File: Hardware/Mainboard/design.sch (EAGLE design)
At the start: 174 parts, among them IC1 STM32H743ZIT6, IC10 DS3231MZ+TRL, IC2 FT312D, IC3 SN74LVC2G241DCUT, IC4 CH340G, IC5 TCA9554APWR, IC6 TCA9554APWR, IC7 TCA9554APWR, IC8 STCC2540, IC9 LM2576HVS-12/NOPB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

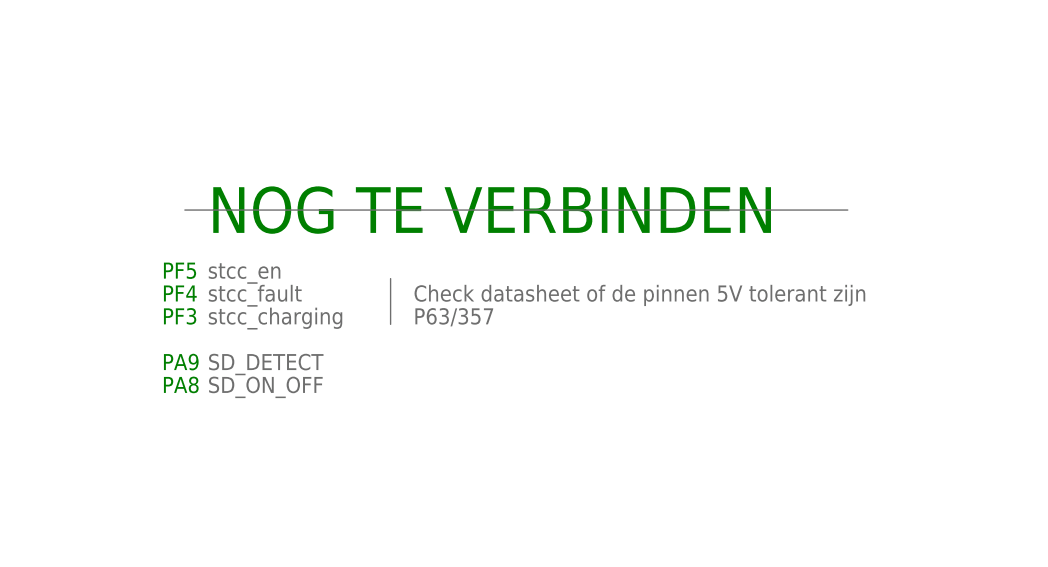
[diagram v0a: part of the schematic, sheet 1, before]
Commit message: Schematics
Add the schematics in pdf format
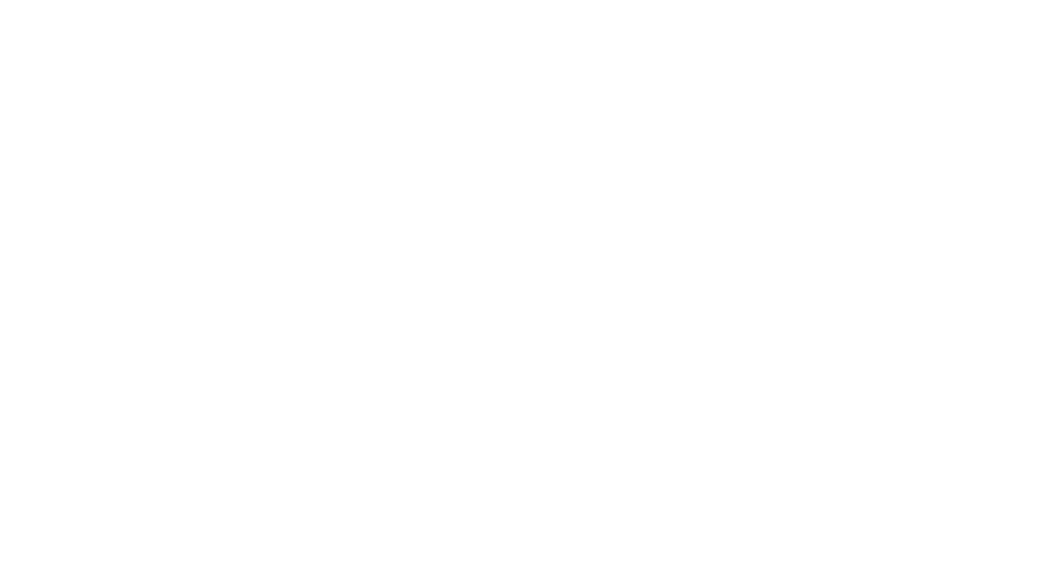
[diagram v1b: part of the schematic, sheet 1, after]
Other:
- note removed: "Check datasheet of de pinnen 5V tolerant zijn"
- note removed: "NOG TE VERBINDEN"
- note removed: "P63/357"
- note removed: "PA8"
- note removed: "PA9"
- note removed: "PF3"
- note removed: "PF4"
- note removed: "PF5"
- note removed: "SD_DETECT"
- note removed: "SD_ON_OFF"
- note removed: "stcc_charging"
- note removed: "stcc_en"
- note removed: "stcc_fault"
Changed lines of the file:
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@@
 <text x="219.71" y="20.32" size="2.54" layer="95">Jarne Van Mulders</text>
 <text x="6.35" y="6.35" size="6.4516" layer="95">DRAMCO</text>
-<text x="284.48" y="76.2" size="5.08" layer="91">NOG TE VERBINDEN</text>
-<text x="284.48" y="71.12" size="1.778" layer="95">stcc_en</text>
-<text x="284.48" y="68.58" size="1.778" layer="95">stcc_fault</text>
-<text x="284.48" y="66.04" size="1.778" layer="95">stcc_charging</text>
-<wire x1="304.8" y1="71.12" x2="304.8" y2="66.04" width="0.1524" layer="95"/>
-<text x="307.34" y="68.58" size="1.778" layer="95">Check datasheet of de pinnen 5V tolerant zijn</text>
-<text x="307.34" y="66.04" size="1.778" layer="95">P63/357</text>
-<text x="284.48" y="60.96" size="1.778" layer="95">SD_DETECT</text>
-<text x="284.48" y="58.42" size="1.778" layer="95">SD_ON_OFF</text>
-<text x="279.4" y="60.96" size="1.778" layer="91">PA9</text>
-<text x="279.4" y="58.42" size="1.778" layer="91">PA8</text>
-<text x="279.4" y="66.04" size="1.778" layer="91">PF3</text>
-<text x="279.4" y="68.58" size="1.778" layer="91">PF4</text>
-<text x="279.4" y="71.12" size="1.778" layer="91">PF5</text>
-<wire x1="281.94" y1="78.74" x2="355.6" y2="78.74" width="0.1524" layer="95"/>
 </plain>
 <instances>
